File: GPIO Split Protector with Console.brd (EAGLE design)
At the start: 93 x 65 mm, 38 parts, among them IC1 DMMT5401, Q1 DMP2305U-7

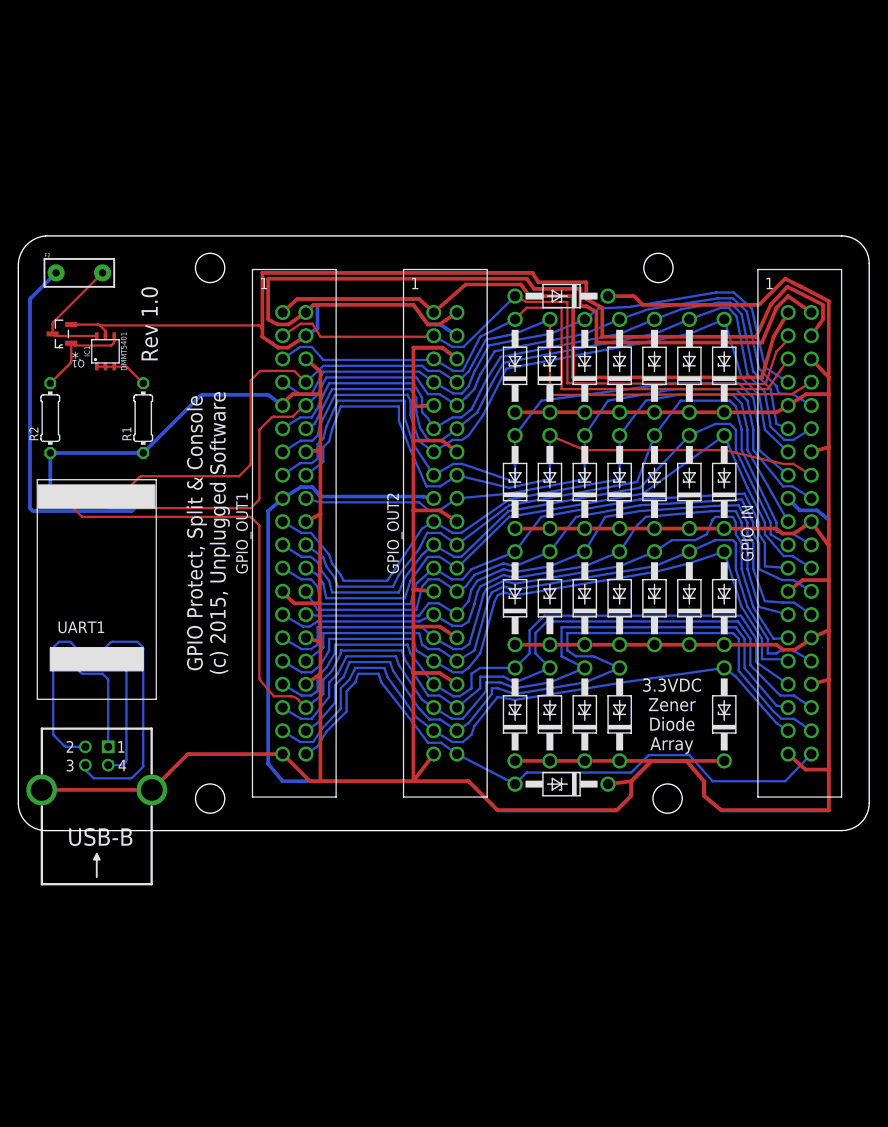
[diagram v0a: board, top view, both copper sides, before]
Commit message: Added printables for split/protect circuit for fab of board.
Added Accessory Relay header to interface board.
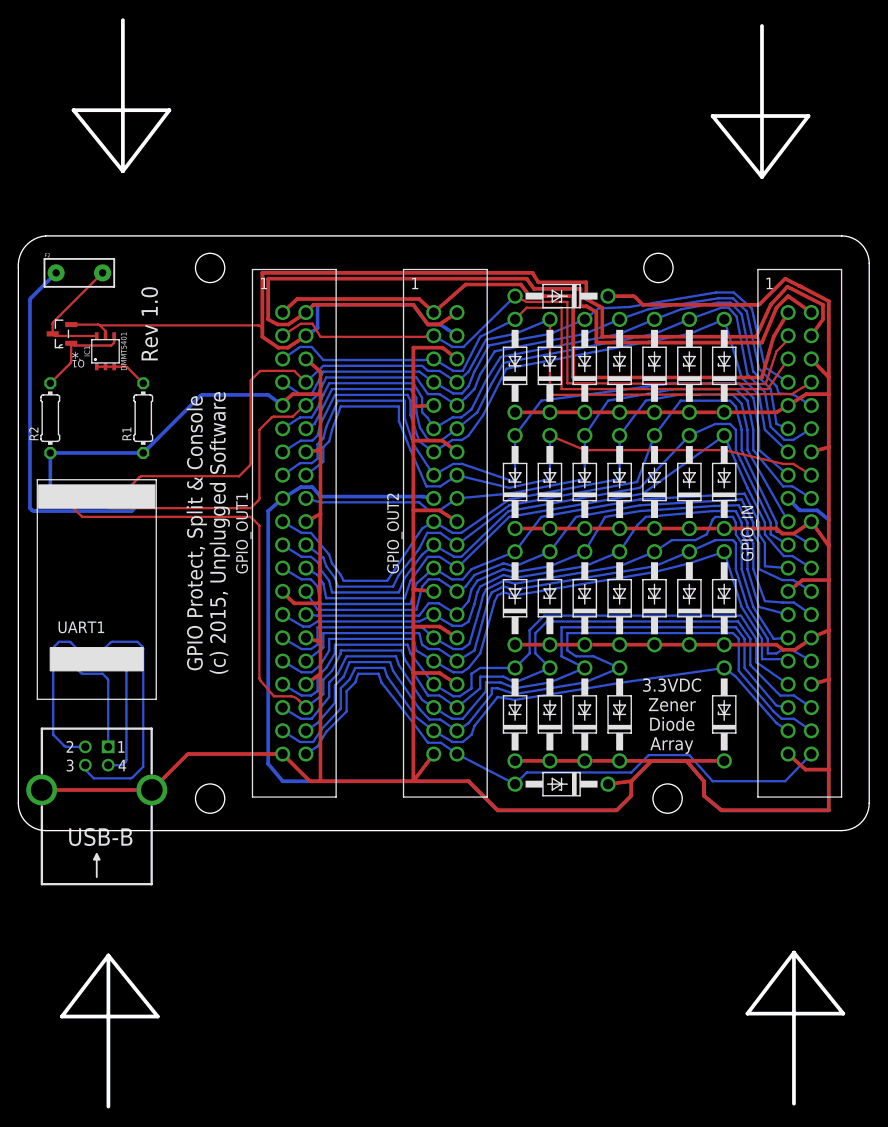
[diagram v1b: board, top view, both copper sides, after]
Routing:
- net GND: track 506.3 -> 501.1 mm
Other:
- board size 93 x 65 mm -> 93 x 118.7 mm
- board text added: "CONSOLE1"
- board text added: "F2"
- board text added: "GPIO_IN"
- board text added: "GPIO_OUT1"
- board text added: "GPIO_OUT2"
- board text added: "IC1"
- board text added: "Q1"
- board text added: "R1"
- board text added: "R2"
- board text added: "UART1"
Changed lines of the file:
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@@
 <grid distance="0.3175" unitdist="mm" unit="mm" style="lines" multiple="1" display="yes" altdistance="0.079375" altunitdist="mm" altunit="mm"/>
 <layers>
-<layer number="1" name="Top" color="4" fill="1" visible="yes" active="yes"/>
+<layer number="1" name="Top" color="4" fill="1" visible="no" active="yes"/>
 <layer number="16" name="Bottom" color="1" fill="1" visible="yes" active="yes"/>
 <layer number="17" name="Pads" color="2" fill="1" visible="yes" active="yes"/>
@@
 <layer number="112" name="tSilk" color="7" fill="1" visible="yes" active="yes"/>
 <layer number="116" name="Patch_BOT" color="9" fill="4" visible="yes" active="yes"/>
-<layer number="121" name="sName" color="7" fill="1" visible="yes" active="yes"/>
+<layer number="121" name="_tPlace" color="14" fill="1" visible="yes" active="yes"/>
 <layer number="122" name="_bPlace" color="7" fill="1" visible="yes" active="yes"/>
-<layer number="123" name="tTestmark" color="7" fill="1" visible="no" active="yes"/>
-<layer number="124" name="bTestmark" color="7" fill="1" visible="no" active="yes"/>
-<layer number="125" name="_tNames" color="7" fill="1" visible="yes" active="yes"/>
+<layer number="123" name="tTestmark" color="7" fill="1" visible="yes" active="yes"/>
+<layer number="124" name="bTestmark" color="7" fill="1" visible="yes" active="yes"/>
+<layer number="125" name="_tNames" color="14" fill="1" visible="yes" active="yes"/>
 <layer number="126" name="_bNames" color="7" fill="1" visible="yes" active="yes"/>
 <layer number="127" name="_tValues" color="7" fill="1" visible="yes" active="yes"/>
 <layer number="128" name="_bValues" color="7" fill="1" visible="yes" active="yes"/>
-<layer number="131" name="tAdjust" color="7" fill="1" visible="no" active="yes"/>
-<layer number="132" name="bAdjust" color="7" fill="1" visible="no" active="yes"/>
+<layer number="131" name="tAdjust" color="7" fill="1" visible="yes" active="yes"/>
+<layer number="132" name="bAdjust" color="7" fill="1" visible="yes" active="yes"/>
 <layer number="144" name="Drill_legend" color="7" fill="1" visible="yes" active="yes"/>
-<layer number="151" name="HeatSink" color="7" fill="1" visible="yes" active="yes"/>
+<layer number="151" name="_tDocu" color="14" fill="1" visible="yes" active="yes"/>
 <layer number="152" name="_bDocu" color="7" fill="1" visible="yes" active="yes"/>
 <layer number="199" name="Contour" color="7" fill="1" visible="yes" active="yes"/>
@@
 <layer number="207" name="207bmp" color="8" fill="10" visible="yes" active="yes"/>
 <layer number="208" name="208bmp" color="9" fill="10" visible="yes" active="yes"/>
-<layer number="209" name="209bmp" color="7" fill="1" visible="no" active="yes"/>
-<layer number="210" name="210bmp" color="7" fill="1" visible="no" active="yes"/>
+<layer number="209" name="209bmp" color="7" fill="1" visible="yes" active="yes"/>
+<layer number="210" name="210bmp" color="7" fill="1" visible="yes" active="yes"/>
 <layer number="211" name="211bmp" color="7" fill="1" visible="yes" active="yes"/>
 <layer number="212" name="212bmp" color="7" fill="1" visible="yes" active="yes"/>
@@
 <wire x1="93" y1="3" x2="90" y2="0" width="0" layer="20" curve="-90"/>
 <text x="15.24" y="50.4825" size="1.778" layer="21" rot="R90"> Rev 1.0</text>
+<text x="13.208" y="1.905" size="1.27" layer="125" ratio="16" rot="R180">CONSOLE1</text>
+<text x="14.6685" y="12.827" size="1.27" layer="125" ratio="16" rot="R180">CONSOLE1</text>
+<text x="9.3345" y="3.937" size="0.762" layer="151" ratio="10" rot="R180">CONSOLE1</text>
+<text x="2.8575" y="62.665" size="0.4318" layer="125">F2</text>
+<text x="80.3275" y="32.5000125" size="1.27" layer="121" rot="R90">GPIO_IN</text>
+<text x="25.0825" y="32.5000125" size="1.27" layer="121" rot="R90">GPIO_OUT1</text>
+<text x="41.5925" y="32.5000125" size="1.27" layer="121" rot="R90">GPIO_OUT2</text>
+<text x="7.825003125" y="52.3875" size="0.6096" layer="125" rot="R90">IC1</text>
+<text x="7.2644" y="51.435" size="0.8128" layer="125" rot="SR180">Q1</text>
+<text x="12.3571" y="42.545" size="0.9906" layer="125" ratio="10" rot="R90">R1</text>
+<text x="2.1971" y="42.545" size="0.9906" layer="125" ratio="10" rot="R90">R2</text>
+<text x="9.525" y="22.86" size="1.27" layer="121" rot="R180">UART1</text>
+<wire x1="11.43" y1="88.5825" x2="11.43" y2="72.0725" width="0.4064" layer="20"/>
+<wire x1="11.43" y1="72.0725" x2="6.0325" y2="78.74" width="0.4064" layer="20"/>
+<wire x1="6.0325" y1="78.74" x2="16.51" y2="78.74" width="0.4064" layer="20"/>
+<wire x1="16.51" y1="78.74" x2="11.43" y2="72.0725" width="0.4064" layer="20"/>
+<wire x1="81.28" y1="87.9475" x2="81.28" y2="71.4375" width="0.4064" layer="20"/>
+<wire x1="81.28" y1="71.4375" x2="75.8825" y2="78.105" width="0.4064" layer="20"/>
+<wire x1="75.8825" y1="78.105" x2="86.36" y2="78.105" width="0.4064" layer="20"/>
+<wire x1="86.36" y1="78.105" x2="81.28" y2="71.4375" width="0.4064" layer="20"/>
+<wire x1="9.8425" y1="-30.1625" x2="9.8425" y2="-13.6525" width="0.4064" layer="20"/>
+<wire x1="9.8425" y1="-13.6525" x2="15.24" y2="-20.32" width="0.4064" layer="20"/>
+<wire x1="15.24" y1="-20.32" x2="4.7625" y2="-20.32" width="0.4064" layer="20"/>
+<wire x1="4.7625" y1="-20.32" x2="9.8425" y2="-13.6525" width="0.4064" layer="20"/>
+<wire x1="84.7725" y1="-29.845" x2="84.7725" y2="-13.335" width="0.4064" layer="20"/>
+<wire x1="84.7725" y1="-13.335" x2="90.17" y2="-20.0025" width="0.4064" layer="20"/>
+<wire x1="90.17" y1="-20.0025" x2="79.6925" y2="-20.0025" width="0.4064" layer="20"/>
+<wire x1="79.6925" y1="-20.0025" x2="84.7725" y2="-13.335" width="0.4064" layer="20"/>
 </plain>
 <attributes>
@@
 <wire x1="61.9125" y1="45.72" x2="58.1025" y2="45.72" width="0.4064" layer="1"/>
 <wire x1="58.1025" y1="45.72" x2="54.2925" y2="45.72" width="0.4064" layer="1"/>
-<wire x1="43.18" y1="52.784375" x2="46.355" y2="52.784375" width="0.4064" layer="16"/>
-<wire x1="46.355" y1="52.784375" x2="47.9425" y2="51.55" width="0.4064" layer="16"/>
 <wire x1="27.305" y1="47.625" x2="28.8925" y2="46.47" width="0.4064" layer="16"/>
 <contactref element="UART1" pad="GND"/>

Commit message: Should have working versions of all required boards now.
Updated to No Commercial license.
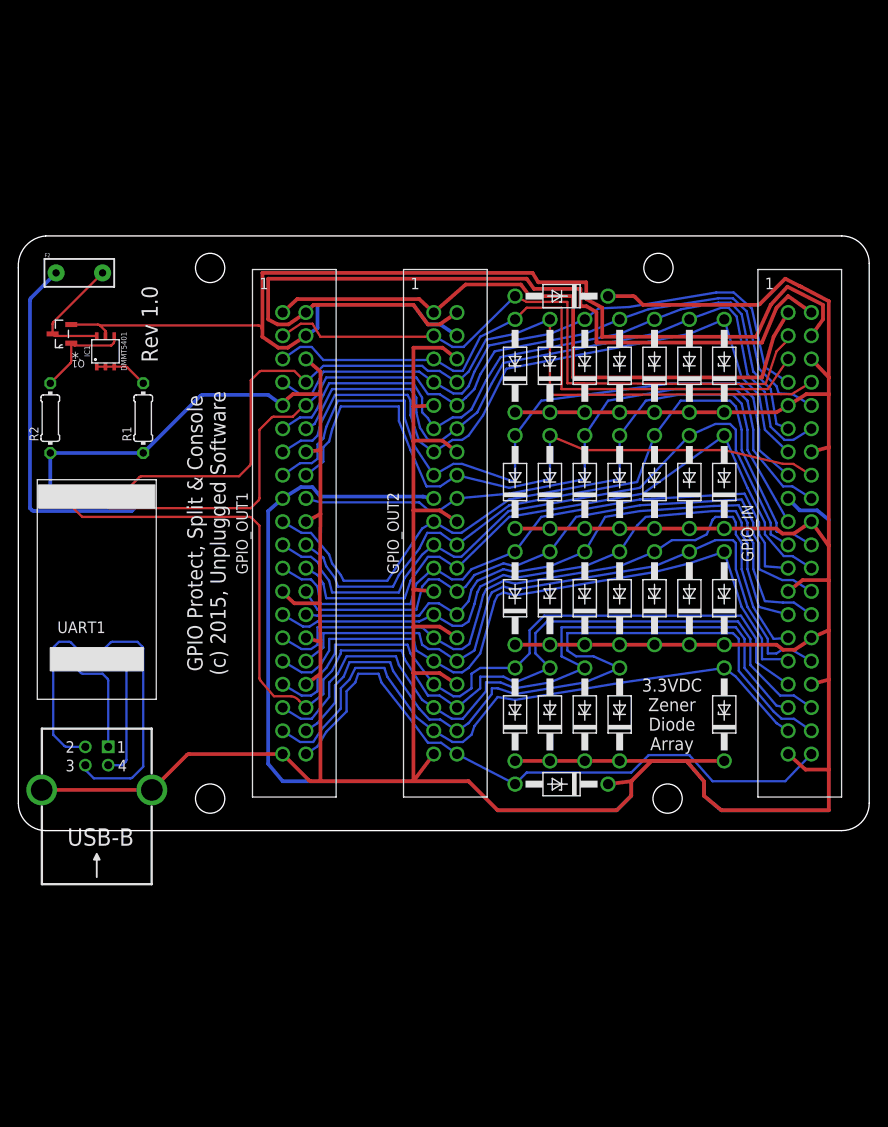
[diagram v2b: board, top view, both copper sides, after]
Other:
- board size 93 x 118.7 mm -> 93 x 65 mm
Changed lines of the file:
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@@
 <grid distance="0.3175" unitdist="mm" unit="mm" style="lines" multiple="1" display="yes" altdistance="0.079375" altunitdist="mm" altunit="mm"/>
 <layers>
-<layer number="1" name="Top" color="4" fill="1" visible="no" active="yes"/>
+<layer number="1" name="Top" color="4" fill="1" visible="yes" active="yes"/>
 <layer number="16" name="Bottom" color="1" fill="1" visible="yes" active="yes"/>
 <layer number="17" name="Pads" color="2" fill="1" visible="yes" active="yes"/>
@@
 <text x="2.1971" y="42.545" size="0.9906" layer="125" ratio="10" rot="R90">R2</text>
 <text x="9.525" y="22.86" size="1.27" layer="121" rot="R180">UART1</text>
-<wire x1="11.43" y1="88.5825" x2="11.43" y2="72.0725" width="0.4064" layer="20"/>
-<wire x1="11.43" y1="72.0725" x2="6.0325" y2="78.74" width="0.4064" layer="20"/>
-<wire x1="6.0325" y1="78.74" x2="16.51" y2="78.74" width="0.4064" layer="20"/>
-<wire x1="16.51" y1="78.74" x2="11.43" y2="72.0725" width="0.4064" layer="20"/>
-<wire x1="81.28" y1="87.9475" x2="81.28" y2="71.4375" width="0.4064" layer="20"/>
-<wire x1="81.28" y1="71.4375" x2="75.8825" y2="78.105" width="0.4064" layer="20"/>
-<wire x1="75.8825" y1="78.105" x2="86.36" y2="78.105" width="0.4064" layer="20"/>
-<wire x1="86.36" y1="78.105" x2="81.28" y2="71.4375" width="0.4064" layer="20"/>
-<wire x1="9.8425" y1="-30.1625" x2="9.8425" y2="-13.6525" width="0.4064" layer="20"/>
-<wire x1="9.8425" y1="-13.6525" x2="15.24" y2="-20.32" width="0.4064" layer="20"/>
-<wire x1="15.24" y1="-20.32" x2="4.7625" y2="-20.32" width="0.4064" layer="20"/>
-<wire x1="4.7625" y1="-20.32" x2="9.8425" y2="-13.6525" width="0.4064" layer="20"/>
-<wire x1="84.7725" y1="-29.845" x2="84.7725" y2="-13.335" width="0.4064" layer="20"/>
-<wire x1="84.7725" y1="-13.335" x2="90.17" y2="-20.0025" width="0.4064" layer="20"/>
-<wire x1="90.17" y1="-20.0025" x2="79.6925" y2="-20.0025" width="0.4064" layer="20"/>
-<wire x1="79.6925" y1="-20.0025" x2="84.7725" y2="-13.335" width="0.4064" layer="20"/>
 </plain>
 <attributes>
